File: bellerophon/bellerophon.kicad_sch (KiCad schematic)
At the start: 1 part

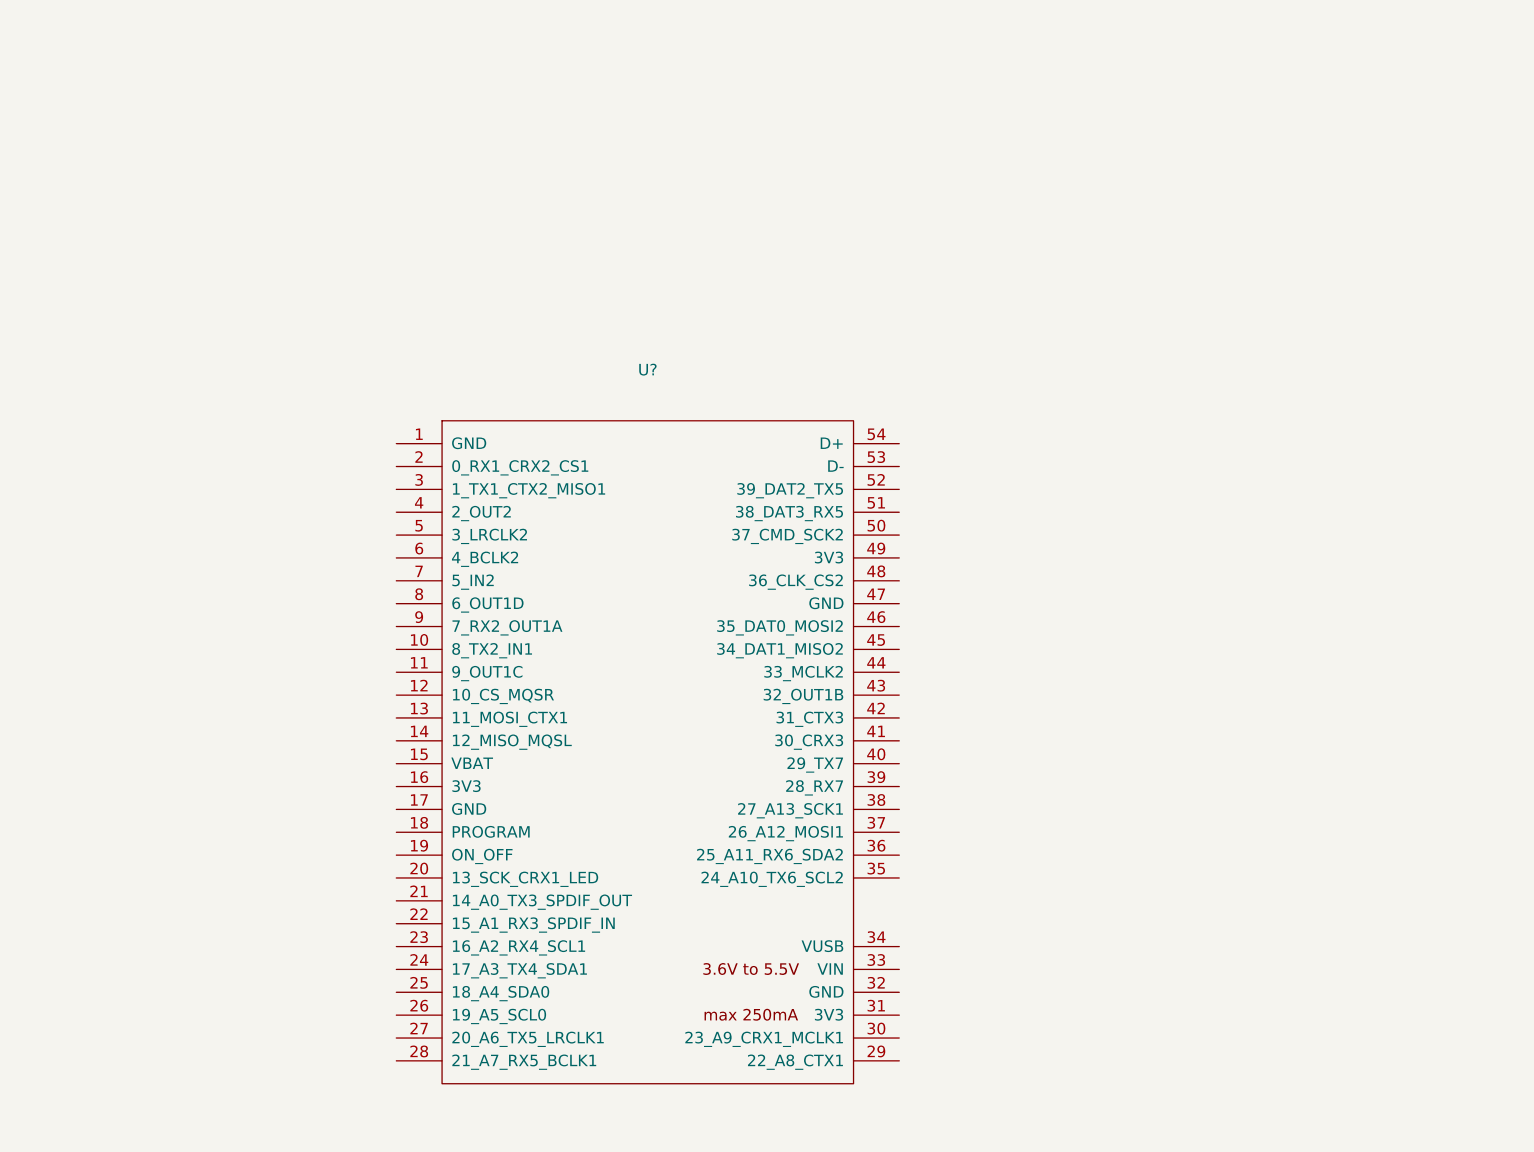
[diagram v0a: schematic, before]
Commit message: added voltage regulator circuitry
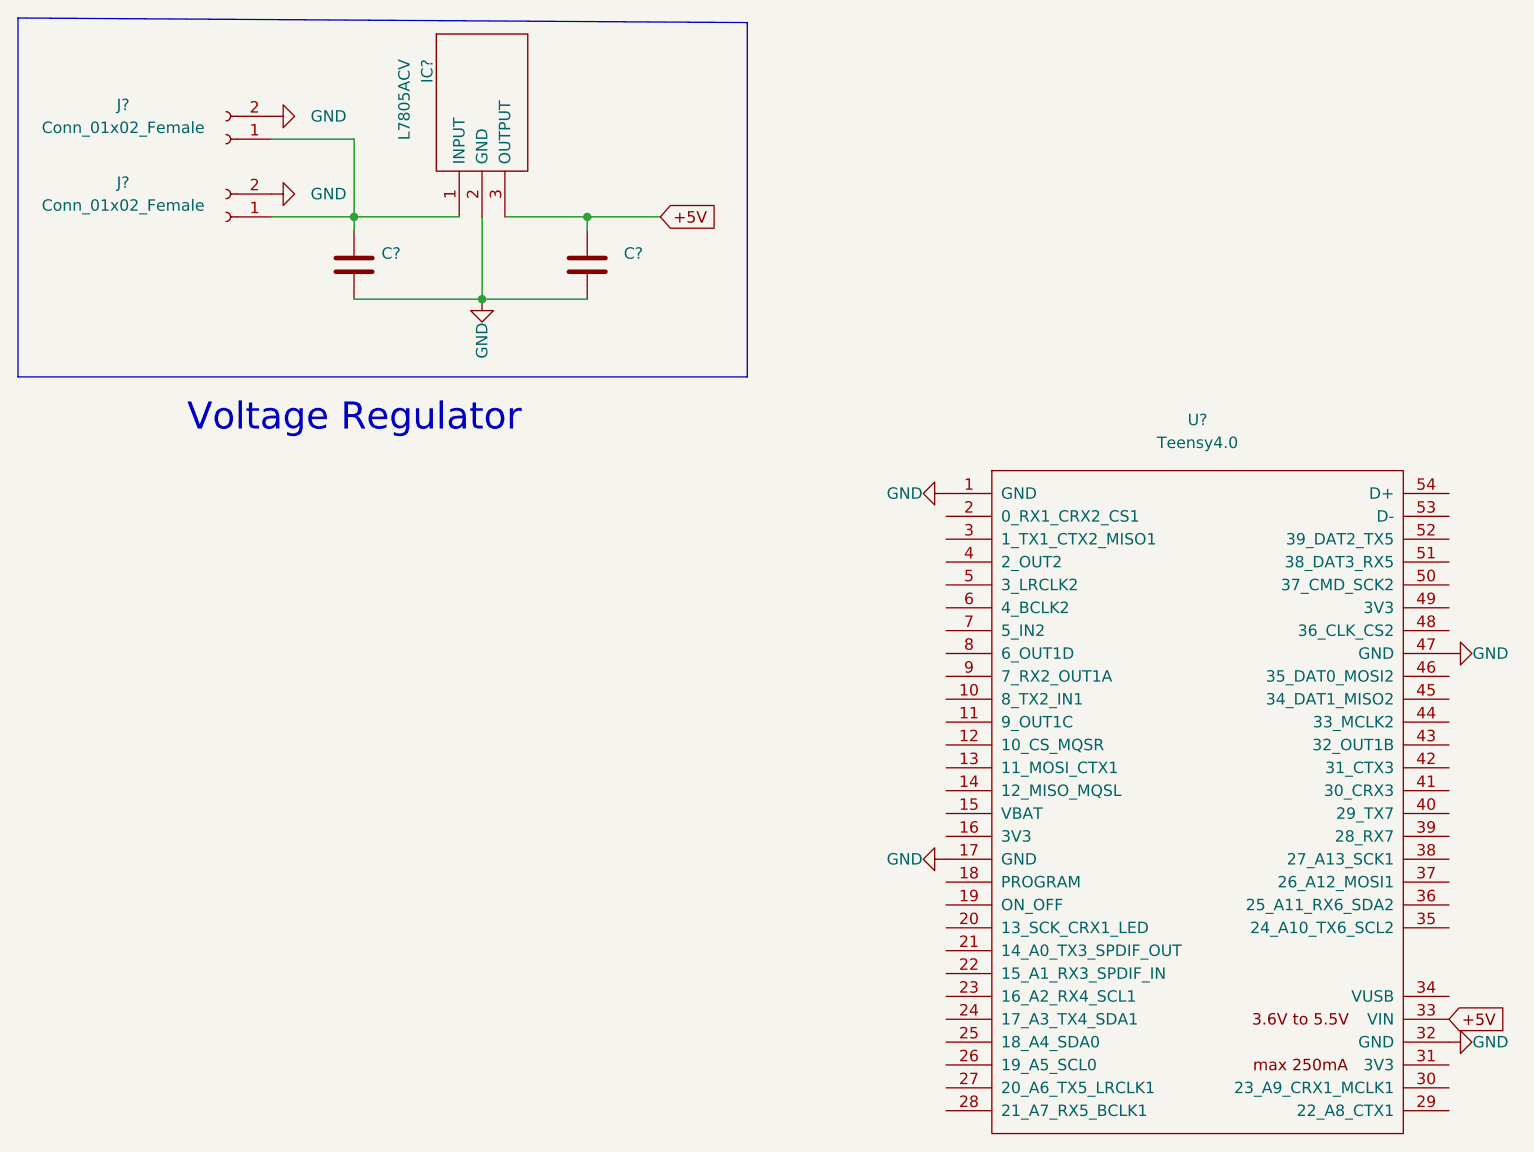
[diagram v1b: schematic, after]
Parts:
- added C? (x2): (no value), symbol Device:C
- added IC?: L7805ACV, TO255P460X1020X2008-3P, symbol Voltage Regulator:L7805ACV
- added J? (x2): Conn_01x02_Female, Connector_PinHeader_2.00mm:PinHeader_1x02_P2.00mm_Vertical, symbol Connector:Conn_01x02_Female
- U?: value (none) -> Teensy4.0
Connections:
- net GND: now reaches U?.1 (GND)
- net GND: now also U?.17 (GND), U?.32 (GND), U?.47 (GND), C?.2, C?.2, IC?.2 (GND), J?.2 (Pin_2), J?.2 (Pin_2)
- net +5V: now reaches U?.33 (VIN)
- net +5V: now also C?.1, IC?.3 (OUTPUT)
- new net: C?.1, IC?.1 (INPUT), J?.1 (Pin_1), J?.1 (Pin_1)
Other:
- note added: "Voltage Regulator"
- moved on the sheet: U?

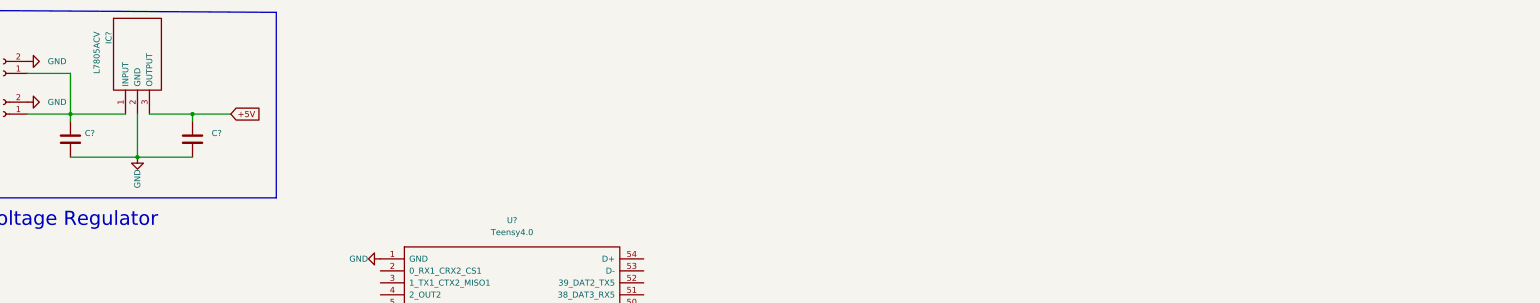
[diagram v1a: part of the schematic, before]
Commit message: added chute deployment mosfets
added chute deployment mosfets
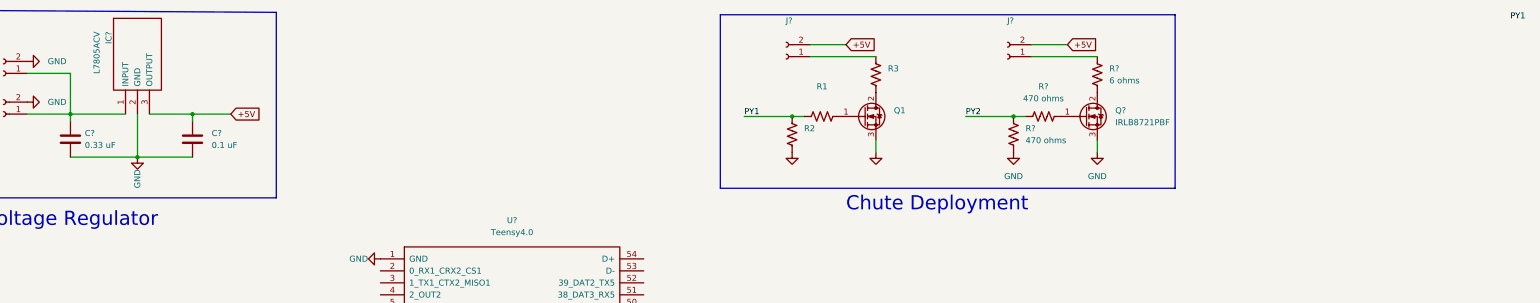
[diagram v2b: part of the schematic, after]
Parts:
- added J? (x2): (no value), symbol Connector:Conn_01x02_Female
- added Q1: (no value), symbol Transistor_FET:IRLB8721PBF
- added Q?: IRLB8721PBF, Package_TO_SOT_THT:TO-220-3_Vertical, symbol Transistor_FET:IRLB8721PBF
- added R1, R2, R3: (no value), symbol Device:R_US
- added R? (x2): 470 ohms, symbol Device:R_US
- added R?: 6 ohms, symbol Device:R_US
- C?: value (none) -> 0.33 uF
- C?: value (none) -> 0.1 uF
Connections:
- net +5V: now also J?.2 (Pin_2), J?.2 (Pin_2)
- net GND: now also Q1.3 (S), Q?.3 (S), R2.1, R?.1
- new net: Q1.1 (G), R1.2
- new net: Q1.2 (D), R3.1
- new net: J?.1 (Pin_1), R?.2
- new net: Q?.1 (G), R?.2
- new net: Q?.2 (D), R?.1
- new net: J?.1 (Pin_1), R3.2
- new net PY1: R1.1, R2.2
- new net PY2: R?.1, R?.2
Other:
- note added: "Chute Deployment"
